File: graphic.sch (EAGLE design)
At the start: 72 parts, among them IC1 NE5532D, IC2 NE5532D, IC3 NE5532D, IC4 NE5532D, IC5 NE5532D, U2 THONKICONNNEW, U3 THONKICONNNEW

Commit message: Simple version PCB complete and routed
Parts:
- removed D1, D2: PMEG2010AEB, diode:DIODE-SOD523
- removed L1, L2: (no value), wuerth-elektronik:WE-CBF_0603
- added C28, C29, C30: 100n, we-rcl:RESISTOR-0805
- added D3, D4: 5819, diode:DIODE-SOD123
- C12, C13, C4, C6, C9: device rcl:C-USC0402 -> we-rcl:RESISTOR-0805
- renumbered U2 to INPUT, U3 to OUTPUT
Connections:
- removed net N$22: D1.C, L1.2
- removed net N$44: D2.A, L2.2
- removed net VCC: C1.1, C13.1, C4.1, C9.1
- removed net VEE: C12.2, C2.2, C6.2
- net +12V: now also C1.1, C13.2, C29.2, C4.2, C9.2, D3.C, IC1P.V+, IC2P.V+, IC3P.V+, IC4P.V+, IC5P.V+; no longer L1.1, R18.2, R19.2, R20.2, R21.2, R22.2, R23.2, R24.2
- net +_INLET: now also D3.A, R18.2, R19.2, R20.2, R21.2, R22.2, R23.2, R24.2; no longer D1.A
- net -12V: now also C12.1, C2.1, C28.1, C30.1, C6.1, D4.A, IC1P.V-, IC2P.V-, IC3P.V-, IC4P.V-, IC5P.V-; no longer L2.1
- net -_INLET: now also D4.C; no longer D2.C
- net GND: now also C12.2, C13.1, C2.2, C28.2, C29.1, C30.2, C4.1, C6.2, C9.1, R11.2, R15.2, R17.2, R7.2; no longer C12.1, C13.2, C2.1, C4.2, C6.1, C9.2, R11.1, R15.1, R17.1, R7.1
- net N$11: now also C17.1; no longer C17.2
- net N$12: now also C15.1, C16.1; no longer C15.2, C16.2
- net N$14: now also C10.1, C8.1; no longer C10.2, C8.2
- net N$16: now also C23.2, IC3A.+IN; no longer C23.1, IC3A.-IN
- net N$17: now also C21.1, C3.2, C7.2; no longer C21.2, C3.1, C7.1
- net N$18: now also C10.2, C8.2, R6.2; no longer C10.1, C8.1, R6.1
- net N$19: now also C18.1, C19.1; no longer C18.2, C19.2
- net N$21: now also IC3A.-IN; no longer IC3A.+IN
- net N$23: now also C20.1; no longer C20.2
- net N$24: now also IC3B.+IN, R11.1; no longer IC3B.-IN, R11.2
- net N$25: now also C21.2, IC2A.+IN; no longer C21.1, IC2A.-IN
- net N$26: now also IC2A.-IN; no longer IC2A.+IN
- net N$27: now also IC3B.-IN, R10.1; no longer IC3B.+IN, R10.2
- net N$28: now also IC2B.+IN, R7.1; no longer IC2B.-IN, R7.2
- net N$29: now also IC2B.-IN, R6.1; no longer IC2B.+IN, R6.2
- net N$3: now also R1.1; no longer R1.2
- net N$30: now also C11.2, C14.2, C23.1; no longer C11.1, C14.1, C23.2
- net N$31: now also C15.2, C16.2, R10.2; no longer C15.1, C16.1, R10.1
- net N$32: now also C25.2, IC4A.+IN; no longer C25.1, IC4A.-IN
- net N$33: now also IC4A.-IN; no longer IC4A.+IN
- net N$34: now also IC4B.+IN, R15.1; no longer IC4B.-IN, R15.2
- net N$35: now also IC4B.-IN, R14.1; no longer IC4B.+IN, R14.2
- net N$36: now also C17.2, C25.1; no longer C17.1, C25.2
- net N$37: now also C18.2, C19.2, R14.2; no longer C18.1, C19.1, R14.1
- net N$38: now also IC5B.+IN, R17.1; no longer IC5B.-IN, R17.2
- net N$39: now also IC5B.-IN, R16.1; no longer IC5B.+IN, R16.2
- net N$4: now also C11.1, C14.1; no longer C11.2, C14.2
- net N$40: now also C20.2, R16.2; no longer C20.1, R16.1
- net N$45: now also R1.2, R26.1; no longer R1.1, R26.2
- net N$5: now also R3.2; no longer R3.1
- net N$6: now also R3.1; no longer R3.2
- net N$8: now also C3.1, C7.1; no longer C3.2, C7.2
- net N$9: now also R26.2; no longer R26.1
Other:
- moved on the sheet: 63HZFADE, IC2A, IC2B, IC3A, IC3B, IC4A, IC4B, IC5B, R1, R25, R26, R3

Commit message: Prototype 1 sent to OSHPark
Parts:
- added C31, C32, C33, C34, C35, C36, C37, C38: NP, we-rcl:CAPACITOR-0805
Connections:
- new net N$22: IC5A.-IN, IC5A.OUT
- net GND: now also IC5A.+IN
- net N$11: now also C34.1, C35.2
- net N$12: now also C33.2
- net N$14: now also C31.1
- net N$18: now also C31.2
- net N$19: now also C36.1
- net N$23: now also C37.1, C38.1
- net N$30: now also C32.1
- net N$31: now also C33.1
- net N$36: now also C34.2, C35.1
- net N$37: now also C36.2
- net N$4: now also C32.2
- net N$40: now also C37.2, C38.2
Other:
- note removed: "!"
- note removed: "6µF @ 11.5V"
- moved on the sheet: C10, C11, C14, C15, C16, C17, C18, C19, C2, C20, C21, C23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

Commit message: updated 20mm fader outlines - NOT moved yet
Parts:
- 160HZ, 16KHZ, 1KHZ, 2.5KHZ, 410HZ, 63HZ, 7.7KHZ: device TomW:ALPHA_20MM_ILLUM_FADER -> MusicThingModular:ALPHA_20MM_ILLUM_FADER
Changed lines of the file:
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@@
 </classes>
 <parts>
-<part name="16KHZ" library="TomW" deviceset="ALPHA_20MM_ILLUM_FADER" device=""/>
-<part name="7.7KHZ" library="TomW" deviceset="ALPHA_20MM_ILLUM_FADER" device=""/>
-<part name="2.5KHZ" library="TomW" deviceset="ALPHA_20MM_ILLUM_FADER" device=""/>
-<part name="1KHZ" library="TomW" deviceset="ALPHA_20MM_ILLUM_FADER" device=""/>
-<part name="410HZ" library="TomW" deviceset="ALPHA_20MM_ILLUM_FADER" device=""/>
-<part name="160HZ" library="TomW" deviceset="ALPHA_20MM_ILLUM_FADER" device=""/>
-<part name="63HZ" library="TomW" deviceset="ALPHA_20MM_ILLUM_FADER" device=""/>
+<part name="16KHZ" library="MusicThingModular" deviceset="ALPHA_20MM_ILLUM_FADER" device=""/>
+<part name="7.7KHZ" library="MusicThingModular" deviceset="ALPHA_20MM_ILLUM_FADER" device=""/>
+<part name="2.5KHZ" library="MusicThingModular" deviceset="ALPHA_20MM_ILLUM_FADER" device=""/>
+<part name="1KHZ" library="MusicThingModular" deviceset="ALPHA_20MM_ILLUM_FADER" device=""/>
+<part name="410HZ" library="MusicThingModular" deviceset="ALPHA_20MM_ILLUM_FADER" device=""/>
+<part name="160HZ" library="MusicThingModular" deviceset="ALPHA_20MM_ILLUM_FADER" device=""/>
+<part name="63HZ" library="MusicThingModular" deviceset="ALPHA_20MM_ILLUM_FADER" device=""/>
 <part name="INPUT" library="MusicThingModular" deviceset="THONKICONN" device="NEW"/>
 <part name="OUTPUT" library="MusicThingModular" deviceset="THONKICONN" device="NEW"/>

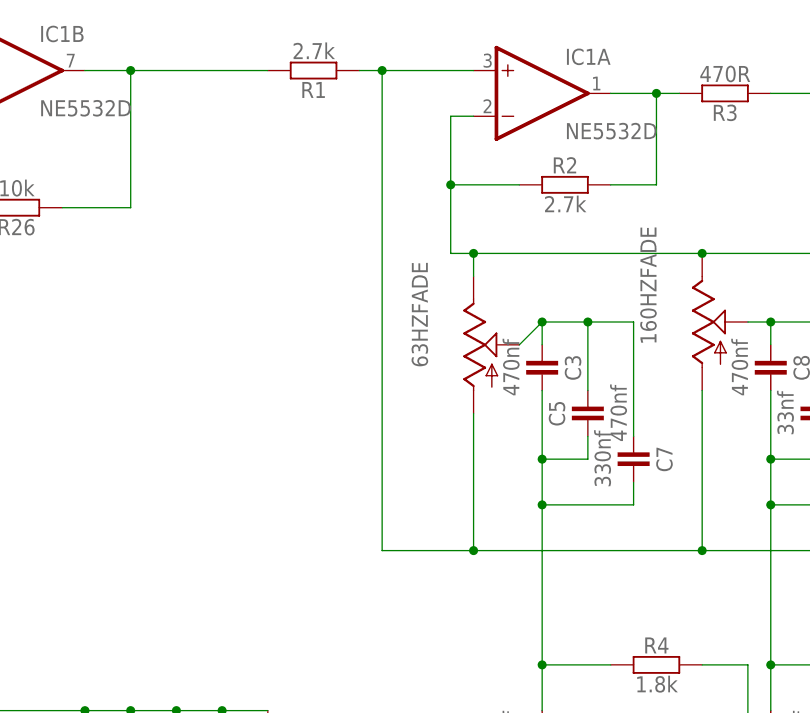
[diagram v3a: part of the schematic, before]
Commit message: move sliders and reverse movement
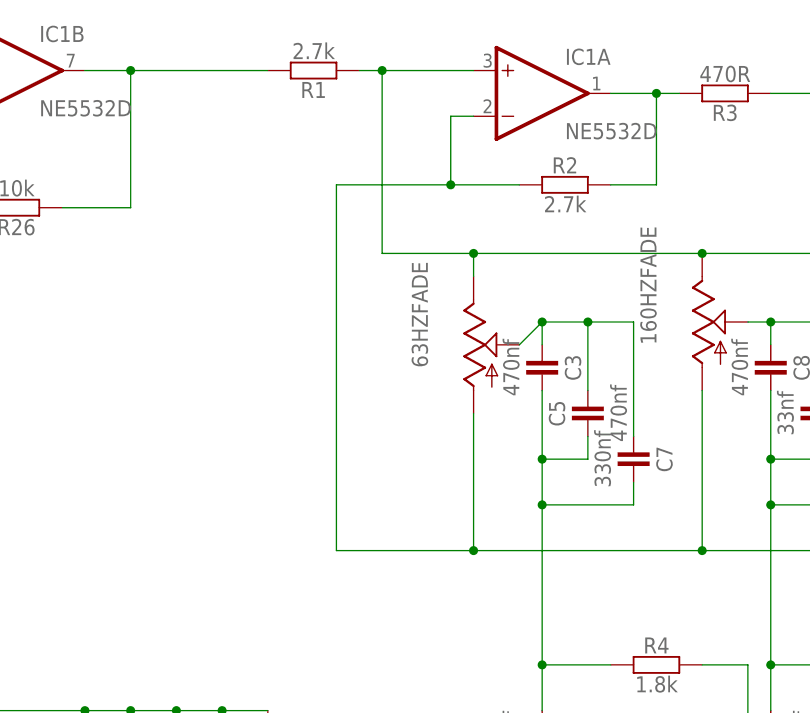
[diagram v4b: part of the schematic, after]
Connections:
- net N$3: now also IC1A.-IN, R2.1; no longer IC1A.+IN, R1.1
- net N$7: now also IC1A.+IN, R1.1; no longer IC1A.-IN, R2.1
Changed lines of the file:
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@@
 <net name="N$3" class="0">
 <segment>
-<pinref part="R1" gate="R" pin="1"/>
-<pinref part="IC1" gate="A" pin="+IN"/>
-<wire x1="33.02" y1="157.48" x2="35.56" y2="157.48" width="0.1524" layer="91"/>
-<wire x1="35.56" y1="157.48" x2="45.72" y2="157.48" width="0.1524" layer="91"/>
-<wire x1="35.56" y1="157.48" x2="35.56" y2="104.14" width="0.1524" layer="91"/>
-<junction x="35.56" y="157.48"/>
 <pinref part="160HZ" gate="FADE" pin="A"/>
 <wire x1="71.12" y1="121.92" x2="71.12" y2="104.14" width="0.1524" layer="91"/>
 <wire x1="71.12" y1="104.14" x2="45.72" y2="104.14" width="0.1524" layer="91"/>
 <pinref part="410HZ" gate="FADE" pin="A"/>
-<wire x1="45.72" y1="104.14" x2="35.56" y2="104.14" width="0.1524" layer="91"/>
+<wire x1="45.72" y1="104.14" x2="30.48" y2="104.14" width="0.1524" layer="91"/>
 <wire x1="99.06" y1="121.92" x2="99.06" y2="104.14" width="0.1524" layer="91"/>
 <wire x1="99.06" y1="104.14" x2="71.12" y2="104.14" width="0.1524" layer="91"/>
@@
 <wire x1="45.72" y1="119.38" x2="45.72" y2="104.14" width="0.1524" layer="91"/>
 <junction x="45.72" y="104.14"/>
+<wire x1="30.48" y1="104.14" x2="30.48" y2="144.78" width="0.1524" layer="91"/>
+<pinref part="IC1" gate="A" pin="-IN"/>
+<wire x1="45.72" y1="152.4" x2="43.18" y2="152.4" width="0.1524" layer="91"/>
+<wire x1="43.18" y1="152.4" x2="43.18" y2="144.78" width="0.1524" layer="91"/>
+<pinref part="R2" gate="R" pin="1"/>
+<wire x1="50.8" y1="144.78" x2="43.18" y2="144.78" width="0.1524" layer="91"/>
+<wire x1="30.48" y1="144.78" x2="43.18" y2="144.78" width="0.1524" layer="91"/>
+<junction x="43.18" y="144.78"/>
 </segment>
 </net>
@@
 <net name="N$7" class="0">
 <segment>
-<pinref part="IC1" gate="A" pin="-IN"/>
-<wire x1="45.72" y1="152.4" x2="43.18" y2="152.4" width="0.1524" layer="91"/>
-<wire x1="43.18" y1="152.4" x2="43.18" y2="144.78" width="0.1524" layer="91"/>
-<pinref part="R2" gate="R" pin="1"/>
-<wire x1="50.8" y1="144.78" x2="43.18" y2="144.78" width="0.1524" layer="91"/>
-<junction x="43.18" y="144.78"/>
-<wire x1="43.18" y1="137.16" x2="43.18" y2="144.78" width="0.1524" layer="91"/>
 <pinref part="16KHZ" gate="FADE" pin="E"/>
 <pinref part="7.7KHZ" gate="FADE" pin="E"/>
@@
 <wire x1="99.06" y1="137.16" x2="71.12" y2="137.16" width="0.1524" layer="91"/>
 <junction x="99.06" y="137.16"/>
-<wire x1="43.18" y1="137.16" x2="45.72" y2="137.16" width="0.1524" layer="91"/>
 <junction x="71.12" y="137.16"/>
 <pinref part="63HZ" gate="FADE" pin="E"/>
@@
 <wire x1="45.72" y1="134.62" x2="45.72" y2="137.16" width="0.1524" layer="91"/>
 <junction x="45.72" y="137.16"/>
-</segment>
-</net>
+<pinref part="IC1" gate="A" pin="+IN"/>
+<pinref part="R1" gate="R" pin="1"/>
+<wire x1="33.02" y1="157.48" x2="35.56" y2="157.48" width="0.1524" layer="91"/>
+<wire x1="35.56" y1="157.48" x2="45.72" y2="157.48" width="0.1524" layer="91"/>
+<wire x1="45.72" y1="137.16" x2="35.56" y2="137.16" width="0.1524" layer="91"/>
+<wire x1="35.56" y1="137.16" x2="35.56" y2="157.48" width="0.1524" layer="91"/>
+<junction x="35.56" y="157.48"/>
+</segment>
+</net>

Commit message: re route and redesign panel
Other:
- moved on the sheet: C32, C33, C35
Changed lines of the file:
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@@
 <instance part="IC5" gate="A" x="322.58" y="88.9"/>
 <instance part="C31" gate="C" x="88.9" y="114.3" rot="R270"/>
-<instance part="C32" gate="C" x="119.38" y="114.3" rot="R270"/>
-<instance part="C33" gate="C" x="152.4" y="111.76" rot="R270"/>
+<instance part="C32" gate="C" x="119.38" y="114.3" rot="R90"/>
+<instance part="C33" gate="C" x="152.4" y="111.76" rot="R90"/>
 <instance part="C34" gate="C" x="185.42" y="119.38" rot="R270"/>
-<instance part="C35" gate="C" x="190.5" y="111.76" rot="R270"/>
+<instance part="C35" gate="C" x="190.5" y="111.76" rot="R90"/>
 <instance part="C36" gate="C" x="236.22" y="111.76" rot="R270"/>
 <instance part="C37" gate="C" x="284.48" y="121.92" rot="R270"/>
@@
 <junction x="106.68" y="129.54"/>
 <pinref part="C32" gate="C" pin="2"/>
-<wire x1="119.38" y1="111.76" x2="119.38" y2="129.54" width="0.1524" layer="91"/>
+<wire x1="119.38" y1="116.84" x2="119.38" y2="129.54" width="0.1524" layer="91"/>
 <wire x1="119.38" y1="129.54" x2="111.76" y2="129.54" width="0.1524" layer="91"/>
 <junction x="111.76" y="129.54"/>
@@
 <pinref part="1KHZ" gate="FADE" pin="S"/>
 <pinref part="C33" gate="C" pin="2"/>
-<wire x1="152.4" y1="109.22" x2="152.4" y2="129.54" width="0.1524" layer="91"/>
+<wire x1="152.4" y1="114.3" x2="152.4" y2="129.54" width="0.1524" layer="91"/>
 <wire x1="152.4" y1="129.54" x2="144.78" y2="129.54" width="0.1524" layer="91"/>
 <junction x="144.78" y="129.54"/>
@@
 <junction x="177.8" y="129.54"/>
 <pinref part="C35" gate="C" pin="2"/>
-<wire x1="190.5" y1="109.22" x2="190.5" y2="129.54" width="0.1524" layer="91"/>
+<wire x1="190.5" y1="114.3" x2="190.5" y2="129.54" width="0.1524" layer="91"/>
 <wire x1="190.5" y1="129.54" x2="185.42" y2="129.54" width="0.1524" layer="91"/>
 <junction x="185.42" y="129.54"/>
@@
 <pinref part="C32" gate="C" pin="1"/>
 <wire x1="106.68" y1="109.22" x2="106.68" y2="114.3" width="0.1524" layer="91"/>
-<wire x1="119.38" y1="116.84" x2="119.38" y2="109.22" width="0.1524" layer="91"/>
+<wire x1="119.38" y1="111.76" x2="119.38" y2="109.22" width="0.1524" layer="91"/>
 <wire x1="119.38" y1="109.22" x2="106.68" y2="109.22" width="0.1524" layer="91"/>
 <junction x="106.68" y="109.22"/>
@@
 <pinref part="C33" gate="C" pin="1"/>
 <wire x1="139.7" y1="106.68" x2="139.7" y2="114.3" width="0.1524" layer="91"/>
-<wire x1="152.4" y1="114.3" x2="152.4" y2="106.68" width="0.1524" layer="91"/>
+<wire x1="152.4" y1="109.22" x2="152.4" y2="106.68" width="0.1524" layer="91"/>
 <wire x1="152.4" y1="106.68" x2="139.7" y2="106.68" width="0.1524" layer="91"/>
 <junction x="139.7" y="106.68"/>
@@
 <junction x="177.8" y="114.3"/>
 <pinref part="C35" gate="C" pin="1"/>
-<wire x1="190.5" y1="114.3" x2="190.5" y2="106.68" width="0.1524" layer="91"/>
+<wire x1="190.5" y1="109.22" x2="190.5" y2="106.68" width="0.1524" layer="91"/>
 <wire x1="190.5" y1="106.68" x2="177.8" y2="106.68" width="0.1524" layer="91"/>
 <junction x="177.8" y="106.68"/>

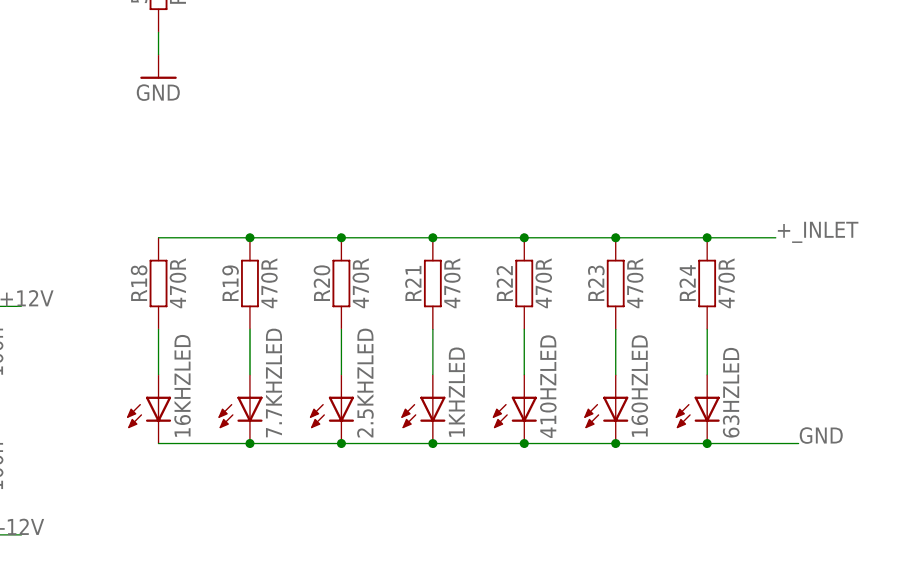
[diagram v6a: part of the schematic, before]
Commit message: Increase LED resistors to reduce current draw
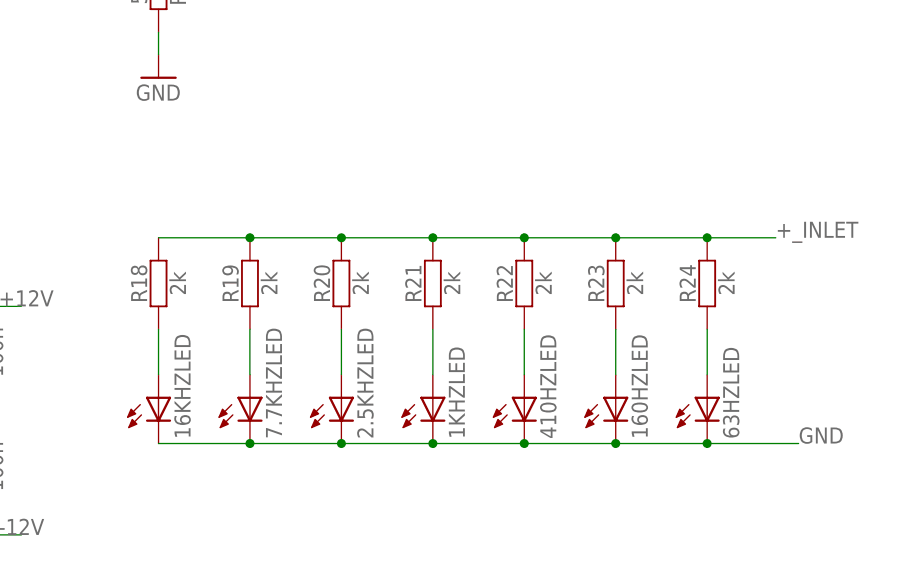
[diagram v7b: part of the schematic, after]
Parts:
- R18, R19, R20, R21, R22, R23, R24: value 470R -> 2k
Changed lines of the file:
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@@
 <?xml version="1.0" encoding="utf-8"?>
 <!DOCTYPE eagle SYSTEM "eagle.dtd">
-<eagle version="7.4.0">
+<eagle version="7.2.0">
 <drawing>
 <settings>
@@
 <part name="R17" library="we-rcl" deviceset="RESISTOR" device="-0805" value="51k"/>
 <part name="GND10" library="SparkFun-Aesthetics" deviceset="GND" device=""/>
-<part name="R18" library="we-rcl" deviceset="RESISTOR" device="-0805" value="470R"/>
-<part name="R19" library="we-rcl" deviceset="RESISTOR" device="-0805" value="470R"/>
-<part name="R20" library="we-rcl" deviceset="RESISTOR" device="-0805" value="470R"/>
-<part name="R21" library="we-rcl" deviceset="RESISTOR" device="-0805" value="470R"/>
-<part name="R22" library="we-rcl" deviceset="RESISTOR" device="-0805" value="470R"/>
-<part name="R23" library="we-rcl" deviceset="RESISTOR" device="-0805" value="470R"/>
-<part name="R24" library="we-rcl" deviceset="RESISTOR" device="-0805" value="470R"/>
+<part name="R18" library="we-rcl" deviceset="RESISTOR" device="-0805" value="2k"/>
+<part name="R19" library="we-rcl" deviceset="RESISTOR" device="-0805" value="2k"/>
+<part name="R20" library="we-rcl" deviceset="RESISTOR" device="-0805" value="2k"/>
+<part name="R21" library="we-rcl" deviceset="RESISTOR" device="-0805" value="2k"/>
+<part name="R22" library="we-rcl" deviceset="RESISTOR" device="-0805" value="2k"/>
+<part name="R23" library="we-rcl" deviceset="RESISTOR" device="-0805" value="2k"/>
+<part name="R24" library="we-rcl" deviceset="RESISTOR" device="-0805" value="2k"/>
 <part name="R25" library="we-rcl" deviceset="RESISTOR" device="-0805" value="10k"/>
 <part name="R26" library="we-rcl" deviceset="RESISTOR" device="-0805" value="10k"/>

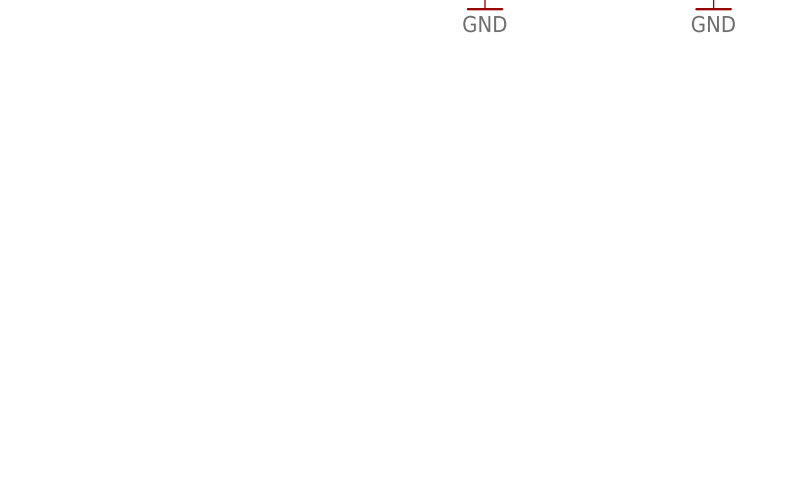
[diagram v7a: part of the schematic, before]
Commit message: Revision 1 board finalised - moved one resistor + added Fiducials
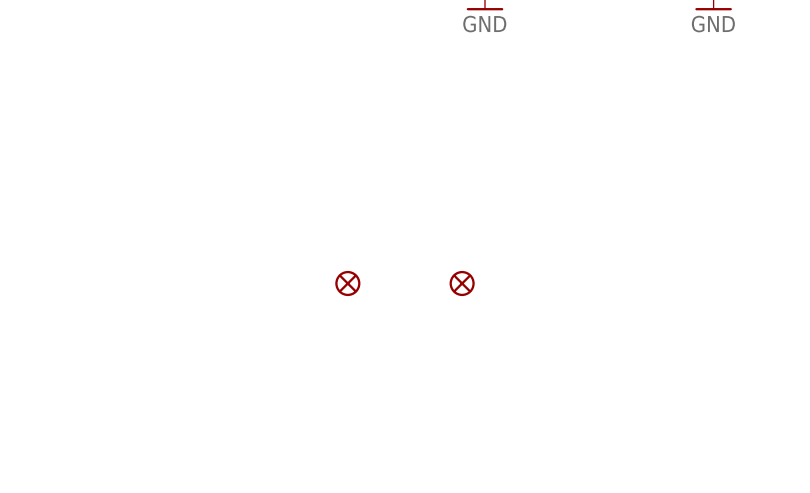
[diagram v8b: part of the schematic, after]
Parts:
- added FID1, FID2: FIDUCIAL1.5X3, SparkFun-Aesthetics:FIDUCIAL1.5X3
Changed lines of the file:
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@@
 <?xml version="1.0" encoding="utf-8"?>
 <!DOCTYPE eagle SYSTEM "eagle.dtd">
-<eagle version="7.2.0">
+<eagle version="7.7.0">
 <drawing>
 <settings>
@@
 <part name="C37" library="we-rcl" deviceset="CAPACITOR" device="-0805" value="NP"/>
 <part name="C38" library="we-rcl" deviceset="CAPACITOR" device="-0805" value="NP"/>
+<part name="FID1" library="SparkFun-Aesthetics" deviceset="FIDUCIAL" device="1.5X3"/>
+<part name="FID2" library="SparkFun-Aesthetics" deviceset="FIDUCIAL" device="1.5X3"/>
 </parts>
 <sheets>
@@
 <instance part="C37" gate="C" x="284.48" y="121.92" rot="R270"/>
 <instance part="C38" gate="C" x="292.1" y="121.92" rot="R270"/>
+<instance part="FID1" gate="G$1" x="38.1" y="27.94"/>
+<instance part="FID2" gate="G$1" x="50.8" y="27.94"/>
 </instances>
 <busses>
